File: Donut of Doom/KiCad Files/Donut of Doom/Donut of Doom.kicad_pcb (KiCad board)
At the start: 2 copper layers, 25 x 53 mm, 48 parts, among them Q1 Q_NMOS_GSD, U3 H3LIS331DLTR, U4 H3LIS331DLTR

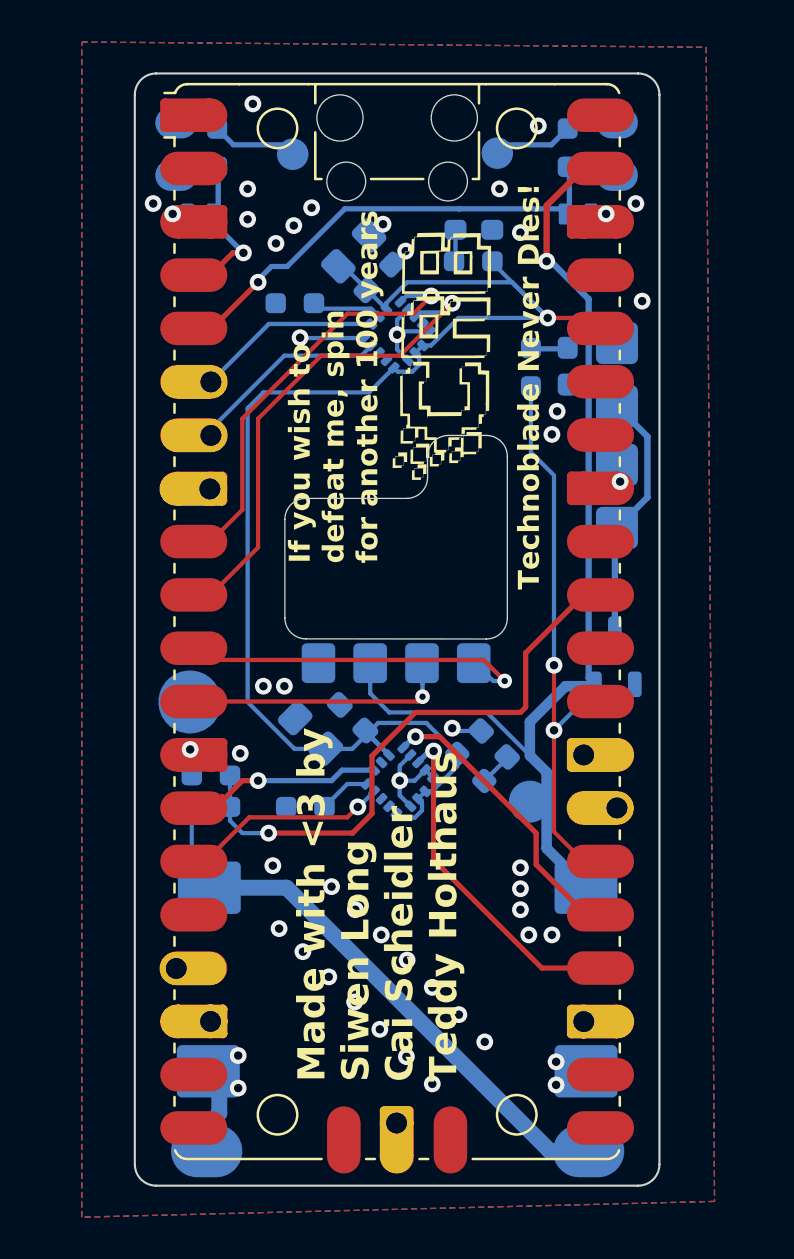
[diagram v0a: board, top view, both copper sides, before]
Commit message: added teardrops
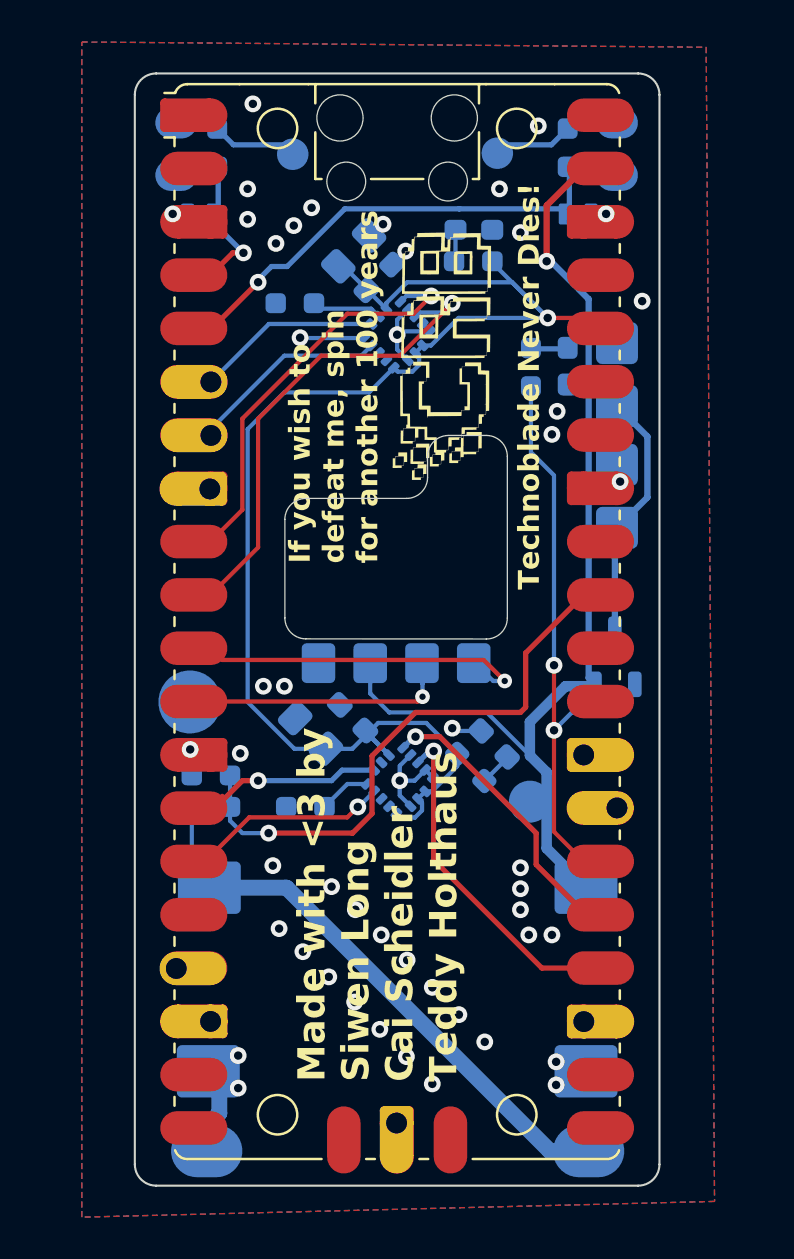
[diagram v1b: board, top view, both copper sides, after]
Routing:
- net +3V3: track 69.9 -> 69.3 mm
- net GND: vias 51 -> 49

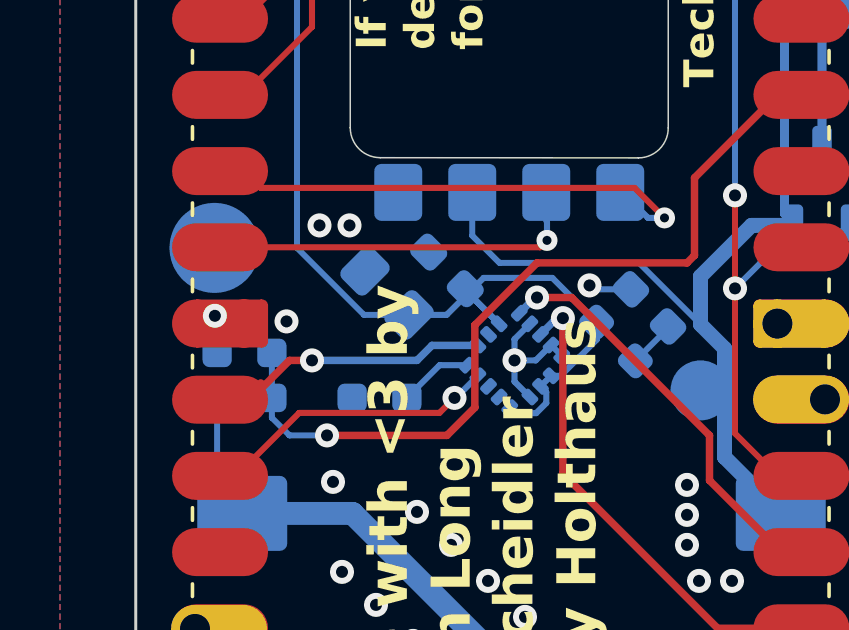
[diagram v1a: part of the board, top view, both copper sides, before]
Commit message: fixed lower accelerameter routing
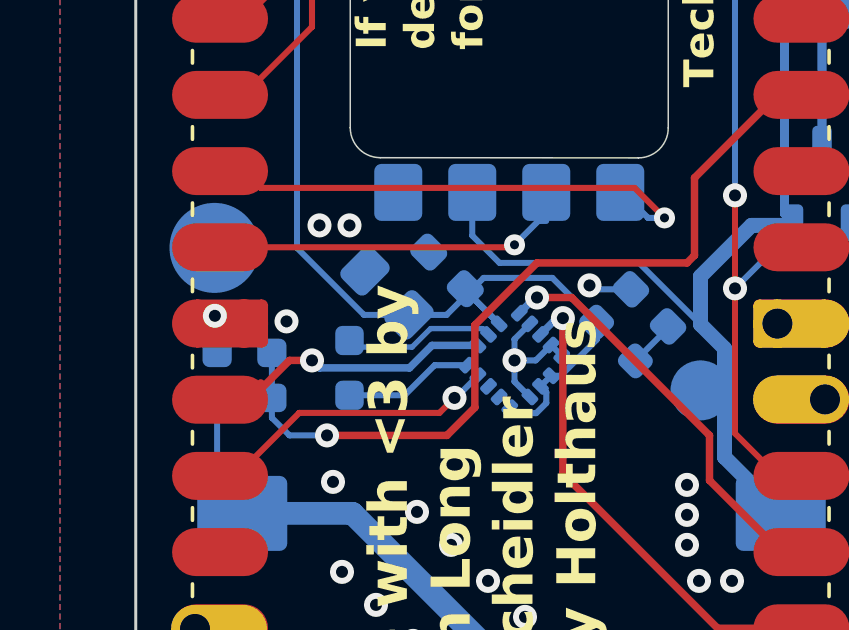
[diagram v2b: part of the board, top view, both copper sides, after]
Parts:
- EX5: value GPIO13 -> IO13
- moved R8 1.41 mm to (145.2, 102.5), turned to 90 degrees
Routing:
- net Net-(U4-SDO/SA0): track 0.00 -> 5.06 mm
- net GND: track 21.5 -> 23.4 mm

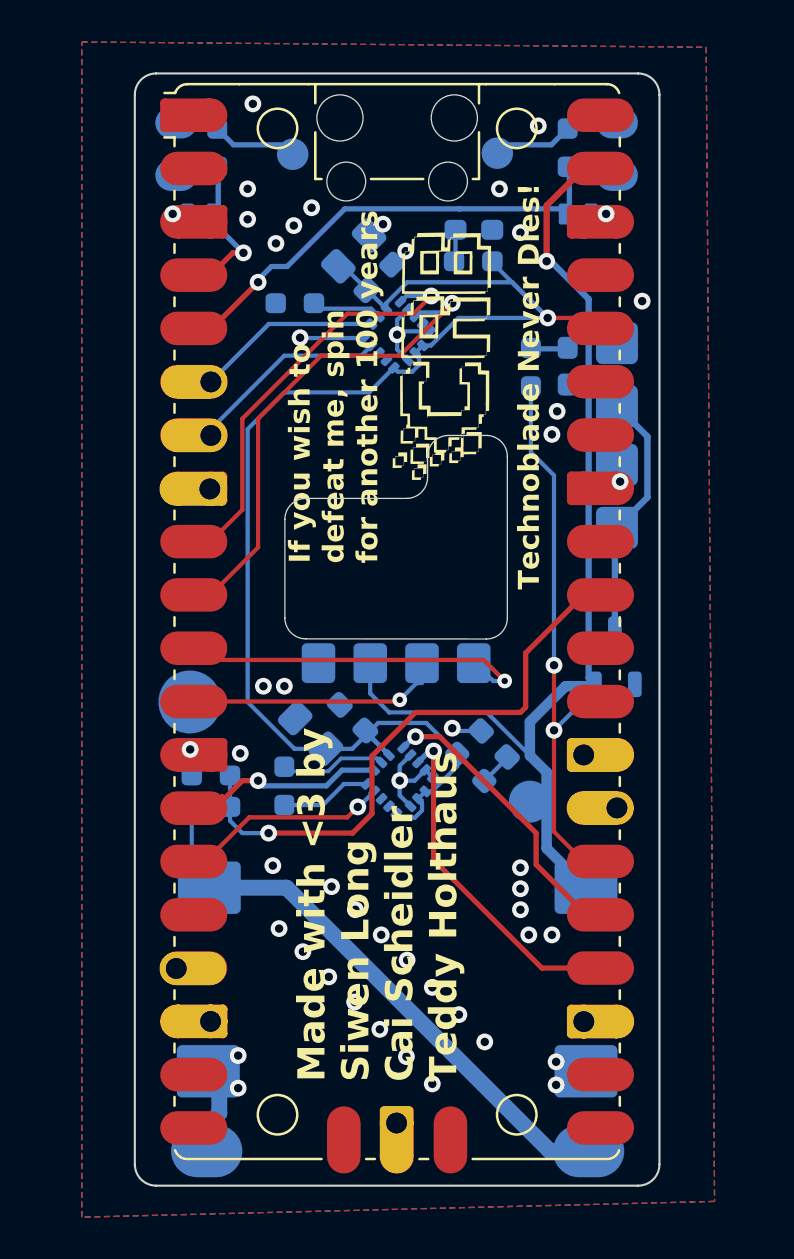
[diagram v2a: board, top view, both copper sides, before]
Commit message: fixed dead copper
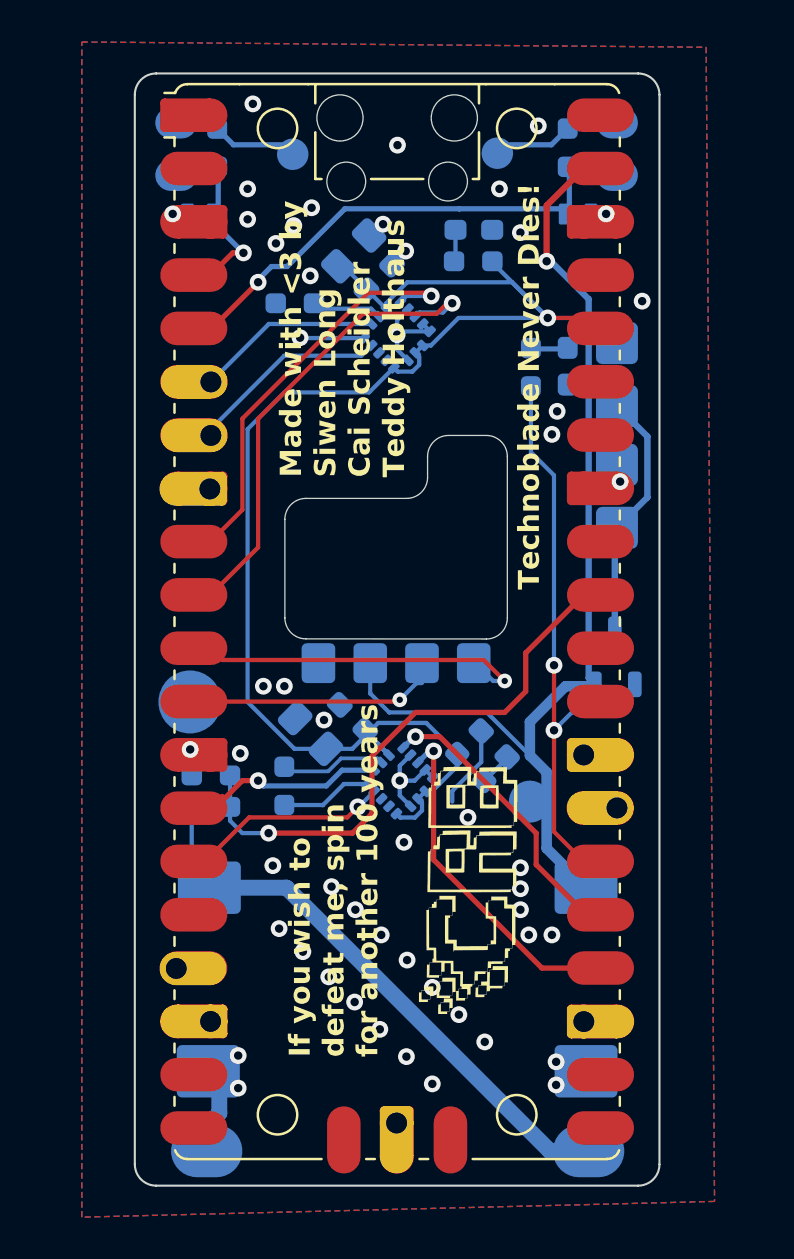
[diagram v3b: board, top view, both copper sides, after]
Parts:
- moved G*** 25.5 mm to (154.0, 107.5)
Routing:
- net GND: track 23.4 -> 25.9 mm, vias 49 -> 53
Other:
- board text removed: "INT2"

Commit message: V3 First rev finished
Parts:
- removed D3: RED 2V LED, LED_SMD:LED_0603_1608Metric_Pad1.05x0.95mm_HandSolder
- removed EX10: GND, Battlebots:Pico_pth_GND
- removed EX7: IO21, Battlebots:Pico_pth_pad
- removed R1: 100, Resistor_SMD:R_0603_1608Metric_Pad0.98x0.95mm_HandSolder
- added G***: LOGO, LOGO, B.Cu at (154.4, 82.8)
- added H1: MountingHole_Pad, MountingHole:MountingHole_2.2mm_M2_DIN965_Pad, F.Cu at (136.2, 71.0)
- added H1: MountingHole_Pad, MountingHole:MountingHole_2.2mm_M2_DIN965_Pad, F.Cu at (165.0, 119.1)
- added JP1: Solder_Jumper, Jumper:SolderJumper-3_P1.3mm_Open_RoundedPad1.0x1.5mm_NumberLabels, B.Cu at (160.4, 94.7)
- moved Q1 4.72 mm to (160.2, 101.0)
- moved D2 2.28 mm to (160.0, 80.9)
- moved D1 1.17 mm to (160.0, 88.3)
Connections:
- A1 pad 27: Net-(A1-GPIO21) -> unconnected-(A1-GPIO21-Pad27)
- D1 pad 1: GND -> Net-(D1-K)
- D2 pad 1: GND -> Net-(D1-K)
- Q1 pad 2: +5V -> GND
- Q1 pad 3: Net-(D1-A) -> Net-(D1-K)
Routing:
- net +BATT: track 28.5 -> 58.8 mm
- net /Directional LED: track 28.8 -> 5.53 mm, vias 2 -> 1
- net Net-(D1-K): track 0.00 -> 23.2 mm
- net +5V: track 49.7 -> 52.6 mm
- net Net-(D1-A): track 12.0 -> 14.5 mm
- net +3V3: track 69.3 -> 66.8 mm
- net Net-(D3-A): track 1.77 -> 0.00 mm
- net GND: vias 53 -> 51
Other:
- board size 25 x 53 mm -> 33.7 x 53 mm
- board text added: "Donut of Doom PCB V3"
- board text added: "LED"
- board text removed: "5VLED"
- board text removed: "Donut of Doom PCB V2"
